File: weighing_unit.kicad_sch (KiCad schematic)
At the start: 0 parts

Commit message: add mcu, sensor, sensor inst, power
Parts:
- added C5, C6: 100n, Capacitor_SMD:C_0805_2012Metric, symbol Device:C
- added D3, D4: BAT60A, Diode_SMD:D_SOD-323, symbol Diode:BAT60A
- added R10, R4, R5: 3k3, Resistor_SMD:R_0805_2012Metric, symbol Device:R
- added R2, R3: 5k, Resistor_SMD:R_0805_2012Metric, symbol Device:R
- added R6: 100, Resistor_SMD:R_0805_2012Metric, symbol Device:R
- added TP1: TestPoint, TestPoint:TestPoint_Pad_D2.5mm, symbol Connector:TestPoint
- added U5: LMV358, Package_SO:SOIC-8_3.9x4.9mm_P1.27mm, symbol Amplifier_Operational:LMV358
- added U6: ADS1115IDGS, Package_SO:TSSOP-10_3x3mm_P0.5mm, symbol Analog_ADC:ADS1115IDGS
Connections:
- new net: R3.2, R5.1, U5.2 (-)
- new net: R5.2, R6.1, U5.1
- new net: R2.2, R4.1, U5.3 (+)
- new net: R10.1, U6.1 (ADDR)
- new net: D3.2 (A), D4.1 (K), R6.2, TP1.1, U6.4 (AIN0)
- new net 3V3: C6.1, D3.1 (K), U6.8 (VDD)
- new net 5V: C5.1, U5.8 (V+)
- new net GND: C6.2, R10.2, U6.3 (GND)
- new net GNDA: C5.2, D4.2 (A), R4.2, U5.4 (V-)
- new net IN1: R2.1
- new net IN2: R3.1
- new net RDY: U6.2 (ALERT/RDY)
- new net SCL: U6.10 (SCL)
- new net SDA: U6.9 (SDA)

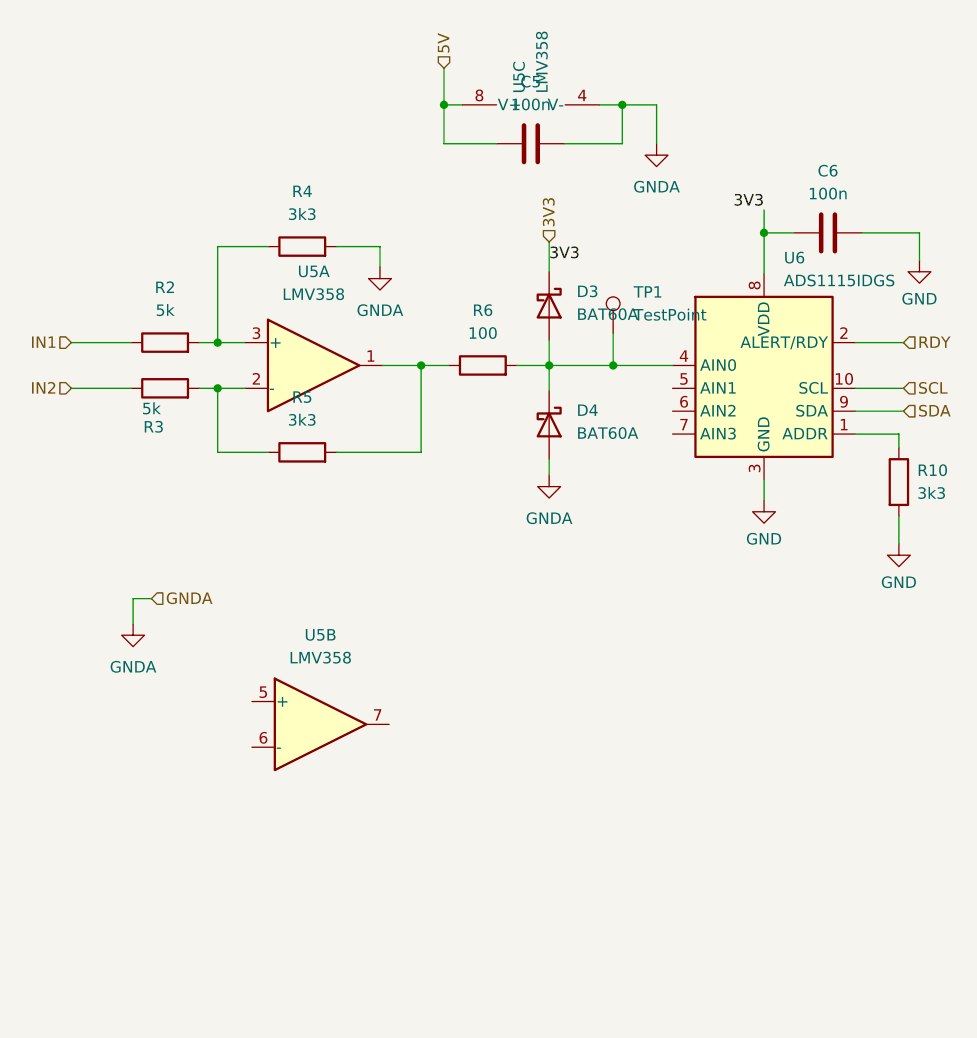
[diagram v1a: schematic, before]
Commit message: add footprint and step
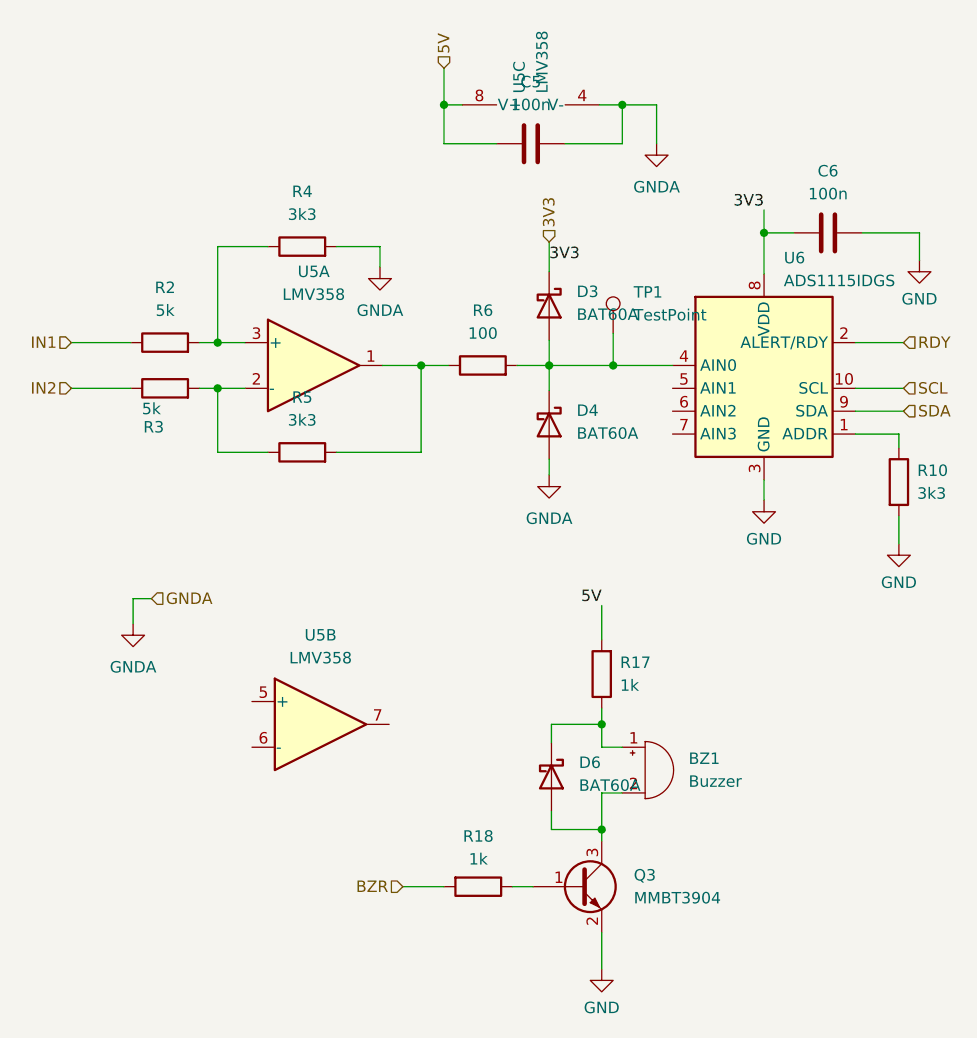
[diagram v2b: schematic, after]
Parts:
- added BZ1: Buzzer, BBG:buzz_14mm_CUI_CEP-1162, symbol Device:Buzzer
- added D6: BAT60A, Diode_SMD:D_SOD-323, symbol Diode:BAT60A
- added Q3: MMBT3904, Package_TO_SOT_SMD:SOT-23, symbol Transistor_BJT:MMBT3904
- added R17, R18: 1k, Resistor_SMD:R_0805_2012Metric, symbol Device:R
- TP1: footprint TestPoint:TestPoint_Pad_D2.5mm -> TestPoint:TestPoint_Pad_D2.0mm
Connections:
- net 5V: now also R17.2
- net GND: now also Q3.2 (E)
- new net: BZ1.1 (+), D6.1 (K), R17.1
- new net: BZ1.2 (-), D6.2 (A), Q3.3 (C)
- new net: Q3.1 (B), R18.1
- new net BZR: R18.2
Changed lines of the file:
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@@
 (kicad_sch (version 20230121) (generator eeschema)
   (paper "A4")
+  (junction (at 112.014 95.504) (diameter 0) (color 0 0 0 0)
+  )
   (junction (at 94.488 26.67) (diameter 0) (color 0 0 0 0)
   )
@@
   (junction (at 130.048 40.894) (diameter 0) (color 0 0 0 0)
   )
+  (junction (at 112.014 107.188) (diameter 0) (color 0 0 0 0)
+  )
   (junction (at 113.284 55.626) (diameter 0) (color 0 0 0 0)
   )
@@
     (stroke (width 0) (type default))
   )
+  (wire (pts (xy 114.3 103.124) (xy 112.014 103.124))
+    (stroke (width 0) (type default))
+  )
   (wire (pts (xy 94.488 26.67) (xy 96.52 26.67))
     (stroke (width 0) (type default))
@@
     (stroke (width 0) (type default))
   )
+  (wire (pts (xy 112.014 118.618) (xy 112.014 122.682))
+    (stroke (width 0) (type default))
+  )
   (wire (pts (xy 140.208 58.166) (xy 145.542 58.166))
     (stroke (width 0) (type default))
@@
     (stroke (width 0) (type default))
   )
+  (wire (pts (xy 112.014 82.296) (xy 112.014 86.106))
+    (stroke (width 0) (type default))
+  )
   (wire (pts (xy 113.284 52.07) (xy 113.284 55.626))
     (stroke (width 0) (type default))
@@
     (stroke (width 0) (type default))
   )
+  (wire (pts (xy 114.3 98.044) (xy 112.014 98.044))
+    (stroke (width 0) (type default))
+  )
   (wire (pts (xy 114.3 30.988) (xy 114.3 26.67))
     (stroke (width 0) (type default))
@@
     (stroke (width 0) (type default))
   )
+  (wire (pts (xy 106.426 97.536) (xy 106.426 95.504))
+    (stroke (width 0) (type default))
+  )
   (wire (pts (xy 106.172 41.91) (xy 106.172 45.212))
     (stroke (width 0) (type default))
@@
     (stroke (width 0) (type default))
   )
+  (wire (pts (xy 112.014 103.124) (xy 112.014 107.188))
+    (stroke (width 0) (type default))
+  )
+  (wire (pts (xy 112.014 95.504) (xy 112.014 93.726))
+    (stroke (width 0) (type default))
+  )
   (wire (pts (xy 147.32 40.894) (xy 147.32 43.942))
     (stroke (width 0) (type default))
@@
     (stroke (width 0) (type default))
   )
+  (wire (pts (xy 106.426 105.156) (xy 106.426 107.188))
+    (stroke (width 0) (type default))
+  )
   (wire (pts (xy 69.342 58.166) (xy 72.39 58.166))
     (stroke (width 0) (type default))
   )
+  (wire (pts (xy 106.426 107.188) (xy 112.014 107.188))
+    (stroke (width 0) (type default))
+  )
+  (wire (pts (xy 102.108 113.538) (xy 104.394 113.538))
+    (stroke (width 0) (type default))
+  )
+  (wire (pts (xy 89.916 113.538) (xy 94.488 113.538))
+    (stroke (width 0) (type default))
+  )
+  (wire (pts (xy 106.426 95.504) (xy 112.014 95.504))
+    (stroke (width 0) (type default))
+  )
   (wire (pts (xy 106.172 55.626) (xy 102.616 55.626))
     (stroke (width 0) (type default))
@@
   )
   (wire (pts (xy 130.048 38.354) (xy 130.048 40.894))
+    (stroke (width 0) (type default))
+  )
+  (wire (pts (xy 112.014 98.044) (xy 112.014 95.504))
+    (stroke (width 0) (type default))
+  )
+  (wire (pts (xy 112.014 107.188) (xy 112.014 108.458))
     (stroke (width 0) (type default))
   )
@@
     (effects (font (size 1.27 1.27)) (justify left bottom))
   )
+  (label "5V" (at 112.014 82.296 180) (fields_autoplaced)
+    (effects (font (size 1.27 1.27)) (justify right bottom))
+  )
   (label "3V3" (at 130.048 38.354 180) (fields_autoplaced)
     (effects (font (size 1.27 1.27)) (justify right bottom))
@@
     (effects (font (size 1.27 1.27)) (justify left))
   )
+  (hierarchical_label "BZR" (shape input) (at 89.916 113.538 180) (fields_autoplaced)
+    (effects (font (size 1.27 1.27)) (justify right))
+  )
   (hierarchical_label "RDY" (shape input) (at 145.542 53.086 0) (fields_autoplaced)
     (effects (font (size 1.27 1.27)) (justify left))
@@
         (path "/8f227bf3-f4cf-485c-a746-8377af835d89/39c2c3b0-4826-42ca-a0df-7d76b180d9b9"
           (reference "R5") (unit 1)
+        )
+      )
+    )
+  )
+  (symbol (lib_id "Diode:BAT60A") (at 106.426 101.346 270) (unit 1)
+    (in_bom yes) (on_board yes) (dnp no) (fields_autoplaced)
+    (property "Reference" "D6" (at 109.474 99.7585 90)
+      (effects (font (size 1.27 1.27)) (justify left))
+    )
+    (property "Value" "BAT60A" (at 109.474 102.2985 90)
+      (effects (font (size 1.27 1.27)) (justify left))
+    )
+    (property "Footprint" "Diode_SMD:D_SOD-323" (at 101.981 101.346 0)
+      (effects (font (size 1.27 1.27)) hide)
+    )
+    (property "Datasheet" "https://www.infineon.com/dgdl/Infineon-BAT60ASERIES-DS-v01_01-en.pdf?fileId=db3a304313d846880113def70c9304a9" (at 106.426 101.346 0)
+      (effects (font (size 1.27 1.27)) hide)
+    )
+    (pin "2")
+    (pin "1")
+    (instances
+      (project "scale"
+        (path "/8f227bf3-f4cf-485c-a746-8377af835d89/39c2c3b0-4826-42ca-a0df-7d76b180d9b9"
+          (reference "D6") (unit 1)
         )
       )
@@
     )
   )
+  (symbol (lib_id "Device:Buzzer") (at 116.84 100.584 0) (unit 1)
+    (in_bom yes) (on_board yes) (dnp no) (fields_autoplaced)
+    (property "Reference" "BZ1" (at 121.666 99.314 0)
+      (effects (font (size 1.27 1.27)) (justify left))
+    )
+    (property "Value" "Buzzer" (at 121.666 101.854 0)
+      (effects (font (size 1.27 1.27)) (justify left))
+    )
+    (property "Footprint" "BBG:buzz_14mm_CUI_CEP-1162" (at 116.205 98.044 90)
+      (effects (font (size 1.27 1.27)) hide)
+    )
+    (property "Datasheet" "~" (at 116.205 98.044 90)
+      (effects (font (size 1.27 1.27)) hide)
+    )
+    (pin "1")
+    (pin "2")
+    (instances
+      (project "scale"
+        (path "/8f227bf3-f4cf-485c-a746-8377af835d89/39c2c3b0-4826-42ca-a0df-7d76b180d9b9"
+          (reference "BZ1") (unit 1)
+        )
+      )
+    )
+  )
   (symbol (lib_id "Device:R") (at 63.5 53.086 90) (unit 1)
     (in_bom yes) (on_board yes) (dnp no) (fields_autoplaced)
@@
       (effects (font (size 1.27 1.27)) (justify left))
     )
-    (property "Footprint" "TestPoint:TestPoint_Pad_D2.5mm" (at 118.364 52.07 0)
+    (property "Footprint" "TestPoint:TestPoint_Pad_D2.0mm" (at 118.364 52.07 0)
       (effects (font (size 1.27 1.27)) hide)
     )
@@
     )
   )
+  (symbol (lib_id "Device:R") (at 112.014 89.916 180) (unit 1)
+    (in_bom yes) (on_board yes) (dnp no) (fields_autoplaced)
+    (property "Reference" "R17" (at 114.046 88.646 0)
+      (effects (font (size 1.27 1.27)) (justify right))
+    )
+    (property "Value" "1k" (at 114.046 91.186 0)
+      (effects (font (size 1.27 1.27)) (justify right))
+    )
+    (property "Footprint" "Resistor_SMD:R_0805_2012Metric" (at 113.792 89.916 90)
+      (effects (font (size 1.27 1.27)) hide)
+    )
+    (property "Datasheet" "~" (at 112.014 89.916 0)
+      (effects (font (size 1.27 1.27)) hide)
+    )
+    (pin "1")
+    (pin "2")
+    (instances
+      (project "scale"
+        (path "/8f227bf3-f4cf-485c-a746-8377af835d89/39c2c3b0-4826-42ca-a0df-7d76b180d9b9"
+          (reference "R17") (unit 1)
+        )
+      )
+    )
+  )
+  (symbol (lib_id "Device:R") (at 98.298 113.538 270) (unit 1)
+    (in_bom yes) (on_board yes) (dnp no) (fields_autoplaced)
+    (property "Reference" "R18" (at 98.298 107.95 90)
+      (effects (font (size 1.27 1.27)))
+    )
+    (property "Value" "1k" (at 98.298 110.49 90)
+      (effects (font (size 1.27 1.27)))
+    )
+    (property "Footprint" "Resistor_SMD:R_0805_2012Metric" (at 98.298 111.76 90)
+      (effects (font (size 1.27 1.27)) hide)
+    )
+    (property "Datasheet" "~" (at 98.298 113.538 0)
+      (effects (font (size 1.27 1.27)) hide)
+    )
+    (pin "1")
+    (pin "2")
+    (instances
+      (project "scale"
+        (path "/8f227bf3-f4cf-485c-a746-8377af835d89/39c2c3b0-4826-42ca-a0df-7d76b180d9b9"
+          (reference "R18") (unit 1)
+        )
+      )
+    )
+  )
   (symbol (lib_id "power:GND") (at 130.048 70.612 0) (unit 1)
     (in_bom yes) (on_board yes) (dnp no) (fields_autoplaced)
@@
         (path "/8f227bf3-f4cf-485c-a746-8377af835d89/39c2c3b0-4826-42ca-a0df-7d76b180d9b9"
           (reference "C6") (unit 1)
+        )
+      )
+    )
+  )
+  (symbol (lib_id "Transistor_BJT:MMBT3904") (at 109.474 113.538 0) (unit 1)
+    (in_bom yes) (on_board yes) (dnp no) (fields_autoplaced)
+    (property "Reference" "Q3" (at 115.57 112.268 0)
+      (effects (font (size 1.27 1.27)) (justify left))
+    )
+    (property "Value" "MMBT3904" (at 115.57 114.808 0)
+      (effects (font (size 1.27 1.27)) (justify left))
+    )
+    (property "Footprint" "Package_TO_SOT_SMD:SOT-23" (at 114.554 115.443 0)
+      (effects (font (size 1.27 1.27) italic) (justify left) hide)
+    )
+    (property "Datasheet" "https://www.onsemi.com/pdf/datasheet/pzt3904-d.pdf" (at 109.474 113.538 0)
+      (effects (font (size 1.27 1.27)) (justify left) hide)
+    )
+    (pin "3")
+    (pin "1")
+    (pin "2")
+    (instances
+      (project "scale"
+        (path "/8f227bf3-f4cf-485c-a746-8377af835d89/39c2c3b0-4826-42ca-a0df-7d76b180d9b9"
+          (reference "Q3") (unit 1)
         )
       )
@@
         )
       )
+    )
+  )
+  (symbol (lib_id "power:GND") (at 112.014 122.682 0) (unit 1)
+    (in_bom yes) (on_board yes) (dnp no) (fields_autoplaced)
+    (property "Reference" "#PWR033" (at 112.014 129.032 0)
+      (effects (font (size 1.27 1.27)) hide)
+    )
+    (property "Value" "GND" (at 112.014 127 0)
+      (effects (font (size 1.27 1.27)))
+    )
+    (property "Footprint" "" (at 112.014 122.682 0)
+      (effects (font (size 1.27 1.27)) hide)
+    )
+    (property "Datasheet" "" (at 112.014 122.682 0)
+      (effects (font (size 1.27 1.27)) hide)
+    )
+    (pin "1")
+    (instances
+      (project "scale"
+        (path "/8f227bf3-f4cf-485c-a746-8377af835d89/39c2c3b0-4826-42ca-a0df-7d76b180d9b9"
+          (reference "#PWR033") (unit 1)
+        )
+      )

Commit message: completing route 1
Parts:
- removed TP1: TestPoint, TestPoint:TestPoint_Pad_D2.0mm, symbol Connector:TestPoint
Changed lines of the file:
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@@
   (junction (at 112.014 107.188) (diameter 0) (color 0 0 0 0)
   )
-  (junction (at 113.284 55.626) (diameter 0) (color 0 0 0 0)
-  )
   (junction (at 69.342 58.166) (diameter 0) (color 0 0 0 0)
   )
@@
     (stroke (width 0) (type default))
   )
-  (wire (pts (xy 113.284 52.07) (xy 113.284 55.626))
-    (stroke (width 0) (type default))
-  )
-  (wire (pts (xy 113.284 55.626) (xy 119.888 55.626))
+  (wire (pts (xy 106.172 55.626) (xy 119.888 55.626))
     (stroke (width 0) (type default))
   )
@@
   )
   (wire (pts (xy 106.172 66.04) (xy 106.172 67.818))
-    (stroke (width 0) (type default))
-  )
-  (wire (pts (xy 106.172 55.626) (xy 113.284 55.626))
     (stroke (width 0) (type default))
   )
@@
         )
       )
-    )
-  )
-  (symbol (lib_id "Connector:TestPoint") (at 113.284 52.07 0) (unit 1)
-    (in_bom yes) (on_board yes) (dnp no) (fields_autoplaced)
-    (property "Reference" "TP1" (at 115.57 47.498 0)
-      (effects (font (size 1.27 1.27)) (justify left))
-    )
-    (property "Value" "TestPoint" (at 115.57 50.038 0)
-      (effects (font (size 1.27 1.27)) (justify left))
-    )
-    (property "Footprint" "TestPoint:TestPoint_Pad_D2.0mm" (at 118.364 52.07 0)
-      (effects (font (size 1.27 1.27)) hide)
-    )
-    (property "Datasheet" "~" (at 118.364 52.07 0)
-      (effects (font (size 1.27 1.27)) hide)
-    )
-    (pin "1")
-    (instances
-      (project "scale"
-        (path "/8f227bf3-f4cf-485c-a746-8377af835d89/39c2c3b0-4826-42ca-a0df-7d76b180d9b9"
-          (reference "TP1") (unit 1)
-        )
-      )

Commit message: start routing
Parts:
- D3, D4, D6: value BAT60A -> SS14; footprint Diode_SMD:D_SOD-323 -> Diode_SMD:D_SMA
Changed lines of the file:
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@@
       (effects (font (size 1.27 1.27)) (justify left))
     )
-    (property "Value" "BAT60A" (at 109.474 102.2985 90)
-      (effects (font (size 1.27 1.27)) (justify left))
-    )
-    (property "Footprint" "Diode_SMD:D_SOD-323" (at 101.981 101.346 0)
+    (property "Value" "SS14" (at 109.474 102.2985 90)
+      (effects (font (size 1.27 1.27)) (justify left))
+    )
+    (property "Footprint" "Diode_SMD:D_SMA" (at 101.981 101.346 0)
       (effects (font (size 1.27 1.27)) hide)
     )
@@
       (effects (font (size 1.27 1.27)) (justify left))
     )
-    (property "Value" "BAT60A" (at 109.22 49.9745 90)
-      (effects (font (size 1.27 1.27)) (justify left))
-    )
-    (property "Footprint" "Diode_SMD:D_SOD-323" (at 101.727 49.022 0)
+    (property "Value" "SS14" (at 109.22 49.9745 90)
+      (effects (font (size 1.27 1.27)) (justify left))
+    )
+    (property "Footprint" "Diode_SMD:D_SMA" (at 101.727 49.022 0)
       (effects (font (size 1.27 1.27)) hide)
     )
@@
       (effects (font (size 1.27 1.27)) (justify left))
     )
-    (property "Value" "BAT60A" (at 109.22 63.1825 90)
-      (effects (font (size 1.27 1.27)) (justify left))
-    )
-    (property "Footprint" "Diode_SMD:D_SOD-323" (at 101.727 62.23 0)
-      (effects (font (size 1.27 1.27)) hide)
-    )
+    (property "Value" "SS14" (at 109.22 63.1825 90)
+      (effects (font (size 1.27 1.27)) (justify left))
+    )
+    (property "Footprint" "Diode_SMD:D_SMA" (at 101.727 62.23 0)
+      (effects (font (size 1.27 1.27)) hide)
+    )
